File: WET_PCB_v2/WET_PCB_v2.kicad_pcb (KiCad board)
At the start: 2 copper layers, 100 x 80 mm, 170 parts, among them J1 Barrel jack, J10 POGO1, J11 Conn_01x09_Pin, J12 Conn_01x09_Pin, J13 Capacitor connector, J14 Capacitor connector, J15 Capacitor connector, J16 Capacitor connector, J17 Capacitor connector, J18 Capacitor connector, J19 Fuse holder or smth to hold t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, J2 Power input, J20 Fuse holder or smth to hold t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, J21 Fuse holder or smth to hold t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, J22 Fuse holder or smth to hold t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, J23 Fuse holder or smth to hold t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, J24 Fuse holder or smth to hold t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, J25 Fuse holder or smth to hold t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, J26 Fuse holder or smth to hold t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, J27 Fuse holder or smth to hold t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, J28 Fuse holder or smth to hold t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, J29 Fuse holder or smth to hold t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, J3 Jumper, J30 Fuse holder or smth to hold t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, J31 LA55_GND, J32 LA55_+, J33 LA55_M, J34 Capacitor connector, J35 Programming, J36 LED_POWER, J4 Coil plug, J5 Vsense_ADC1_IN1, J6 Pluggable Terminal Block, J7 Conn_01x09_Pin, J8 Conn_01x09_Pin, J9 POGO2, Q1 IRF530NPBF, Q2 IRF530NPBF, Q3 IRF530NPBF, Q4 IRF530NPBF, Q5 Q_NMOS_GDS, Q6 Q_NMOS_GDS, U1 Opamp_Quad, U3 IR2110, U4 IR2110, U5 IR2110, U6 L7805, U7 LA55-P

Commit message: routing for things that matter done
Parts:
- D20: moved to F.Cu
- moved D20 5.15 mm to (248.8, 94.9), turned to 180 degrees
- moved R20 3.93 mm to (194.2, 143.2), turned to 0 degrees
- moved D6 0.53 mm to (207.8, 132.8)
- moved C2 0.29 mm to (209.9, 105.7)
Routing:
- net +12V: track 3.85 -> 217.2 mm, vias 0 -> 2
- net Net-(U1D-in4+): track 1.80 -> 27.1 mm
- net /DCDC/currsense_FET_side: track 72.7 -> 79.9 mm
- net Net-(D14-K): track 16.5 -> 20.3 mm
- net /DCDC/DCDC_coil_circuit_side: track 0.00 -> 3.75 mm
- net Net-(U1D-in4-): track 29.8 -> 31.5 mm
- net Net-(J16-Pin_2): track 36.5 -> 38.1 mm
- net /inverter/Inv_Driver_Right_SD: track 3.28 -> 2.72 mm
- net Net-(D6-K): track 11.8 -> 11.3 mm
- added copper zone on F.Cu, net +12V

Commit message: updates to routing
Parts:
- moved D21 4.60 mm to (174.1, 163.0)
- moved R61 0.50 mm to (247.5, 106.5)
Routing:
- net /ADC1_IN4: track 14.6 -> 25.3 mm
- net Net-(D7-K): track 32.6 -> 36.5 mm
- net /USART2_TX: track 0.00 -> 3.89 mm
- net /USART2_RX: track 0.00 -> 3.89 mm
- net /TIM17_CH1N: track 54.6 -> 58.5 mm
- net /TIM17_CH1: track 55.1 -> 59.0 mm
- net /SYS_NRST: track 0.00 -> 3.89 mm
- net /GPIO_PC15: track 0.00 -> 3.89 mm
- net /ADC1_IN1: track 8.34 -> 12.2 mm
- net /ADC1_IN0: track 12.4 -> 16.3 mm
- net /DCDC/VoutDCDC: vias 0 -> 12
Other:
- board text added: "Aqua Verde DCDC + Inverter board"

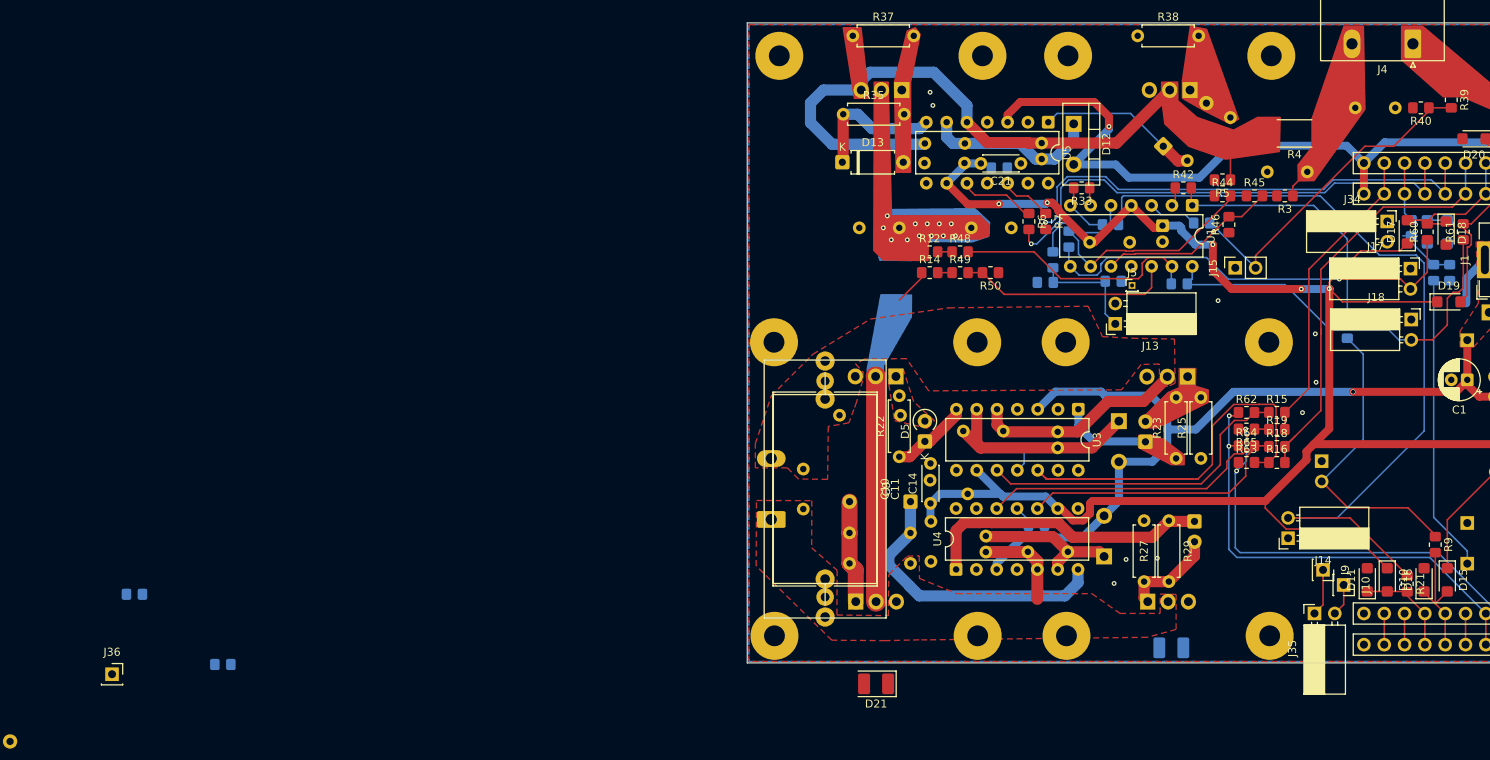
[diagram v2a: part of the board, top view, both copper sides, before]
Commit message: fixed some mistakes added debug header
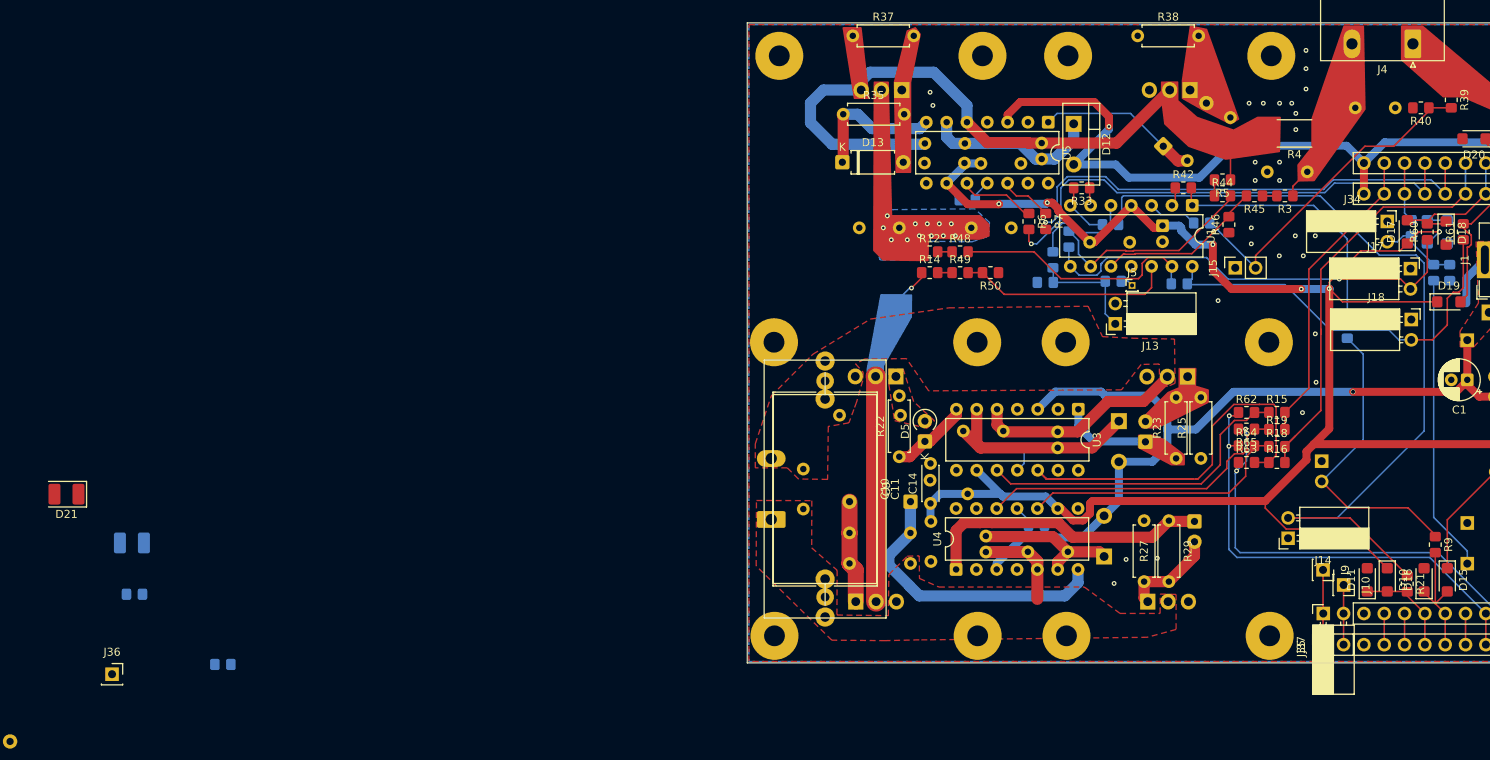
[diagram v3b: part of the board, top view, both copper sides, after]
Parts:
- added J37: Programming, Connector_PinSocket_2.54mm:PinSocket_1x02_P2.54mm_Vertical, F.Cu at (230.0, 158.1)
- C21: moved to B.Cu
- moved D23 130.6 mm to (81.1, 145.4)
- moved D21 103.9 mm to (72.9, 139.3)
- moved R8 5.66 mm to (185.5, 102.5), turned to 180 degrees
- moved J35 1.10 mm to (230.0, 154.2)
- turned R45 to 180 degrees
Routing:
- net +5V: track 236.6 -> 243.3 mm, vias 5 -> 7
- net Net-(J35-Pin_1): track 5.88 -> 9.35 mm
- net Net-(J10-Pin_1): track 4.02 -> 7.47 mm
- net /DCDC/DCDC_Driver_SD: track 0.00 -> 2.71 mm
- net Net-(J34-Pin_2): track 7.82 -> 10.1 mm
- net /currsense_DCDC/Shunt_to_load: track 0.00 -> 2.00 mm
- net /currsense_DCDC/Shunt_from_source: track 0.00 -> 1.80 mm
- net Net-(U1C-in3+): track 22.6 -> 20.9 mm
- net /voltsense_inverter/Vsense_in: track 0.00 -> 1.57 mm
- net /inverter/Vin_Inverter: track 32.9 -> 33.4 mm, vias 0 -> 1
- net GND: vias 9 -> 28
- added copper zone on B.Cu, net /DCDC/VoutDCDC

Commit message: labels
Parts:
- C10, C8, C9: value B32529C1104K000 -> C_inv_out
- C11: value C -> C_inv_out
- J35, J37: value Programming -> PRGM_DBG
- renumbered R3 to JMP1, R15 to JMP10, R16 to JMP11, R17 to JMP12, R18 to JMP13, R19 to JMP14, R64 to JMP15, R20 to JMP16, R65 to JMP17, R33 to JMP18, R21 to JMP19, R5 to JMP2, R42 to JMP20, R9 to JMP21, R60 to JMP22, R61 to JMP23, R10 to JMP24, R6 to JMP3, R7 to JMP4, R8 to JMP5, R12 to JMP6, R14 to JMP7, R62 to JMP8, R63 to JMP9
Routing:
- net GND: vias 28 -> 37
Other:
- board text added: "ADC0"
- board text added: "ADC1"
- board text added: "ADC16"
- board text added: "ADC4"
- board text added: "ADC5"
- board text added: "C9-11"
- board text added: "G D S"
- board text added: "OPAMP ADC1"
- board text added: "OPAMP ADC????"
- board text added: "TIM17"
- board text added: "TIM3"
- board text added: "add pinout of mcu here"
- board text added: "filter cap"
- board text added: "shunt"

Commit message: finished and added some drawings
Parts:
- removed J25, J26, J28: Fuse holder or smth to hold tube, TestPoint:TestPoint_Loop_D2.60mm_Drill0.9mm_Beaded
- added G***: LOGO, LOGO, F.Cu at (220.3, 112.3)
- added G***: LOGO, LOGO, F.Cu at (172.2, 139.0)
- added G***: LOGO, LOGO, B.Cu at (252.1, 87.3)
- added G***: LOGO, LOGO, B.Cu at (220.1, 112.3)
- added H1: MountingScrew, MountingHole:MountingHole_3.2mm_M3_ISO14580, F.Cu at (245.8, 137.1)
- added H2: MountingScrew, MountingHole:MountingHole_3.2mm_M3_ISO14580, F.Cu at (218.6, 146.8)
- added H3: MountingScrew, MountingHole:MountingHole_3.2mm_M3_ISO14580, F.Cu at (165.8, 101.1)
- added J39: TEST, Connector_PinSocket_2.54mm:PinSocket_1x01_P2.54mm_Vertical, F.Cu at (229.5, 90.5)
- added J40: TEST, Connector_PinSocket_2.54mm:PinSocket_1x01_P2.54mm_Vertical, F.Cu at (221.0, 93.8)
- added J41: TEST, Connector_PinSocket_2.54mm:PinSocket_1x01_P2.54mm_Vertical, F.Cu at (248.6, 87.4)
- added J43: PRGM_DBG, Connector_PinSocket_2.54mm:PinSocket_1x02_P2.54mm_Vertical, F.Cu at (168.5, 112.5)
- added J44: GND, Connector_PinSocket_2.54mm:PinSocket_1x01_P2.54mm_Vertical, F.Cu at (167.2, 109.5)
- added J45: PRGM_DBG, Connector_PinSocket_2.54mm:PinSocket_1x02_P2.54mm_Vertical, B.Cu at (167.7, 139.9)
- added J46: GND, Connector_PinSocket_2.54mm:PinSocket_1x01_P2.54mm_Vertical, F.Cu at (207.2, 97.0)
- added J47: GND, Connector_PinSocket_2.54mm:PinSocket_1x01_P2.54mm_Vertical, F.Cu at (249.9, 82.5)
- added MNT10: Fuse holder or smth to hold tube, TestPoint:TestPoint_Loop_D2.60mm_Drill0.9mm_Beaded, F.Cu at (255.5, 151.5)
- D1, D2: footprint LED_THT:LED_D3.0mm -> LED_SMD:LED_PLCC-2_3.4x3.0mm_AK
- D22, D23, D24, D25, D26, R52, R53, R54, R55, R56, R57: moved to F.Cu
- MNT1: renamed from J19; moved to F.Cu
- MNT11: renamed from J29; moved to F.Cu
- MNT12: renamed from J30; moved to F.Cu
- MNT2: renamed from J20; moved to F.Cu
- MNT3: renamed from J21; moved to F.Cu
- MNT4: renamed from J22; moved to F.Cu
- MNT5: renamed from J23; moved to F.Cu
- MNT9: renamed from J27; moved to F.Cu
- moved MNT12 202.9 mm to (255.5, 139.8), turned to 0 degrees
- moved R56 189.6 mm to (203.8, 82.0)
- moved MNT4 185.7 mm to (217.8, 158.2), turned to 90 degrees
- moved MNT5 179.7 mm to (228.2, 85.2)
- moved R53 176.0 mm to (217.8, 152.8), turned to 0 degrees
- moved D23 174.5 mm to (255.6, 147.8), turned to 90 degrees
- moved R54 170.6 mm to (252.0, 149.2), turned to 180 degrees
- moved D25 170.6 mm to (205.8, 85.3), turned to 0 degrees
- moved MNT11 161.8 mm to (192.8, 85.2), turned to 90 degrees
- moved D22 160.7 mm to (213.2, 158.2)
- moved MNT1 155.3 mm to (192.2, 158.5), turned to 90 degrees
- moved D1 150.3 mm to (244.0, 130.2), turned to 180 degrees
- moved J36 147.5 mm to (225.5, 148.8)
- moved R1 144.2 mm to (247.5, 130.0), turned to -90 degrees
- moved R52 140.9 mm to (181.5, 158.8), turned to 0 degrees
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- renumbered J24 to MNT6
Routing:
- net /decoration/UVLED1: track 0.00 -> 248.5 mm, vias 0 -> 5
- net /inverter/Vin_Inverter: track 33.5 -> 13.5 mm
- net /DCDC/VoutDCDC: track 2.82 -> 14.5 mm
- net Net-(D22-A): track 0.00 -> 6.75 mm
- net /DCDC/currsense_FET_side: track 79.9 -> 76.1 mm, vias 0 -> 1
- net Net-(D25-A): track 0.00 -> 3.49 mm
- net Net-(J17-Pin_2): track 55.8 -> 58.9 mm
- net /TIM17_CH1: track 59.0 -> 56.0 mm
- net /TIM17_CH1N: track 58.5 -> 55.5 mm
- net +12V: track 217.2 -> 219.9 mm
- net Net-(D23-A): track 0.00 -> 2.62 mm
- net Net-(D26-A): track 0.00 -> 2.52 mm
- net Net-(D21-A): track 0.00 -> 2.52 mm
- net Net-(D24-A): track 0.00 -> 2.52 mm
- net Net-(D2-A): track 0.00 -> 2.41 mm
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- added copper zone on F.Cu, net /DCDC/DCDC_coil_circuit_side
- added copper zone on F.Cu, net /DCDC/Gatedriver/Q1_gate
- added copper zone on F.Cu, net /DCDC/Gatedriver/Q2_gate
- added copper zone on F.Cu, net /DCDC/VoutDCDC
- added copper zone on F.Cu, net /DCDC/currsense_FET_side
- added copper zone on F.Cu, net /inverter/Vin_Inverter
- added copper zone on F.Cu, net Net-(D6-A)
- added copper zone on F.Cu, net Net-(D6-K)
- added copper zone on F.Cu, net VPP
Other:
- board text added: "12V"
- board text added: "5V"
- board text added: "Aqua Verde"
- board text added: "GND"
- board text added: "LEDs"
- board text added: "OPAMP ADC0"
- board text added: "coil/Vin"
- board text added: "coil/shunt"
- board text added: "test shunt"
- board text removed: "OPAMP ADC????"
- board text removed: "add pinout of mcu here"

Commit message: finisg?
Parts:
- added G***: LOGO, LOGO, B.Cu at (174.3, 106.0)
- moved MNT3 0.96 mm to (167.1, 158.9)
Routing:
- net Net-(JMP20-Pad2): track 33.8 -> 32.2 mm
- net /decoration/UVLED1: track 248.5 -> 247.3 mm
- net GND: vias 92 -> 107
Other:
- board text added: "Raf van Mil, Jake Voets, Oliwia Hejduk, Radman Mustafa, Joshua van Sandijk, Fintan Rising, Lara Korink Romani, Max Schraven"
